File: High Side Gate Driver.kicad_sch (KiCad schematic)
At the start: 12 parts, among them U4 BQ76200PW

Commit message: worked on MCU
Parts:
- renumbered C46 to C21, C53 to C22, C55 to C23, R135 to R54, R138 to R55, R139 to R56, R140 to R57, R141 to R58, R142 to R59, R147 to R60, R148 to R61, U4 to U2
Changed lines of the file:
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@@
 		(on_board yes)
 		(dnp no)
-		(property "Reference" "R148"
+		(property "Reference" "R61"
 			(at 174.752 104.14 90)
 			(effects
@@
 			(project "Project-Star"
 				(path "/fc8533bc-25dd-4c20-9b4c-ffebebd6739b/e8da5d81-614b-4fe5-84b3-4c351fab7114/0c1979a3-247e-411f-a48d-22d4cf657d3e"
-					(reference "R148")
+					(reference "R61")
 					(unit 1)
 				)
@@
 		(on_board yes)
 		(dnp no)
-		(property "Reference" "#FLG06"
+		(property "Reference" "#FLG02"
 			(at 114.935 77.47 0)
 			(effects
@@
 			(project "Project-Star"
 				(path "/fc8533bc-25dd-4c20-9b4c-ffebebd6739b/e8da5d81-614b-4fe5-84b3-4c351fab7114/0c1979a3-247e-411f-a48d-22d4cf657d3e"
-					(reference "#FLG06")
+					(reference "#FLG02")
 					(unit 1)
 				)
@@
 		(on_board yes)
 		(dnp no)
-		(property "Reference" "#PWR079"
+		(property "Reference" "#PWR09"
 			(at 109.22 120.65 0)
 			(effects
@@
 			(project "Project-Star"
 				(path "/fc8533bc-25dd-4c20-9b4c-ffebebd6739b/e8da5d81-614b-4fe5-84b3-4c351fab7114/0c1979a3-247e-411f-a48d-22d4cf657d3e"
-					(reference "#PWR079")
+					(reference "#PWR09")
 					(unit 1)
 				)
@@
 		(on_board yes)
 		(dnp no)
-		(property "Reference" "C53"
+		(property "Reference" "C22"
 			(at 165.1 81.534 90)
 			(effects
@@
 			(project "Project-Star"
 				(path "/fc8533bc-25dd-4c20-9b4c-ffebebd6739b/e8da5d81-614b-4fe5-84b3-4c351fab7114/0c1979a3-247e-411f-a48d-22d4cf657d3e"
-					(reference "C53")
+					(reference "C22")
 					(unit 1)
 				)
@@
 		(on_board yes)
 		(dnp no)
-		(property "Reference" "R141"
+		(property "Reference" "R58"
 			(at 133.604 109.22 90)
 			(effects
@@
 			(project "Project-Star"
 				(path "/fc8533bc-25dd-4c20-9b4c-ffebebd6739b/e8da5d81-614b-4fe5-84b3-4c351fab7114/0c1979a3-247e-411f-a48d-22d4cf657d3e"
-					(reference "R141")
+					(reference "R58")
 					(unit 1)
 				)
@@
 		(on_board yes)
 		(dnp no)
-		(property "Reference" "#PWR081"
+		(property "Reference" "#PWR010"
 			(at 158.75 128.27 0)
 			(effects
@@
 			(project "Project-Star"
 				(path "/fc8533bc-25dd-4c20-9b4c-ffebebd6739b/e8da5d81-614b-4fe5-84b3-4c351fab7114/0c1979a3-247e-411f-a48d-22d4cf657d3e"
-					(reference "#PWR081")
+					(reference "#PWR010")
 					(unit 1)
 				)
@@
 		(on_board yes)
 		(dnp no)
-		(property "Reference" "R147"
+		(property "Reference" "R60"
 			(at 174.752 101.6 90)
 			(effects
@@
 			(project "Project-Star"
 				(path "/fc8533bc-25dd-4c20-9b4c-ffebebd6739b/e8da5d81-614b-4fe5-84b3-4c351fab7114/0c1979a3-247e-411f-a48d-22d4cf657d3e"
-					(reference "R147")
+					(reference "R60")
 					(unit 1)
 				)
@@
 		(on_board yes)
 		(dnp no)
-		(property "Reference" "R142"
+		(property "Reference" "R59"
 			(at 147.574 81.28 90)
 			(effects
@@
 			(project "Project-Star"
 				(path "/fc8533bc-25dd-4c20-9b4c-ffebebd6739b/e8da5d81-614b-4fe5-84b3-4c351fab7114/0c1979a3-247e-411f-a48d-22d4cf657d3e"
-					(reference "R142")
+					(reference "R59")
 					(unit 1)
 				)
@@
 		(on_board yes)
 		(dnp no)
-		(property "Reference" "#PWR057"
+		(property "Reference" "#PWR011"
 			(at 177.8 82.55 0)
 			(effects
@@
 			(project "Project-Star"
 				(path "/fc8533bc-25dd-4c20-9b4c-ffebebd6739b/e8da5d81-614b-4fe5-84b3-4c351fab7114/0c1979a3-247e-411f-a48d-22d4cf657d3e"
-					(reference "#PWR057")
+					(reference "#PWR011")
 					(unit 1)
 				)
@@
 		(on_board yes)
 		(dnp no)
-		(property "Reference" "#PWR012"
+		(property "Reference" "#PWR08"
 			(at 109.22 81.28 0)
 			(effects
@@
 			(project "Project-Star"
 				(path "/fc8533bc-25dd-4c20-9b4c-ffebebd6739b/e8da5d81-614b-4fe5-84b3-4c351fab7114/0c1979a3-247e-411f-a48d-22d4cf657d3e"
-					(reference "#PWR012")
+					(reference "#PWR08")
 					(unit 1)
 				)
@@
 		(on_board yes)
 		(dnp no)
-		(property "Reference" "C46"
+		(property "Reference" "C21"
 			(at 109.22 93.218 0)
 			(effects
@@
 			(project "Project-Star"
 				(path "/fc8533bc-25dd-4c20-9b4c-ffebebd6739b/e8da5d81-614b-4fe5-84b3-4c351fab7114/0c1979a3-247e-411f-a48d-22d4cf657d3e"
-					(reference "C46")
+					(reference "C21")
 					(unit 1)
 				)
@@
 		(on_board yes)
 		(dnp no)
-		(property "Reference" "R139"
+		(property "Reference" "R56"
 			(at 133.604 104.14 90)
 			(effects
@@
 			(project "Project-Star"
 				(path "/fc8533bc-25dd-4c20-9b4c-ffebebd6739b/e8da5d81-614b-4fe5-84b3-4c351fab7114/0c1979a3-247e-411f-a48d-22d4cf657d3e"
-					(reference "R139")
+					(reference "R56")
 					(unit 1)
 				)
@@
 		(on_board yes)
 		(dnp no)
-		(property "Reference" "#FLG05"
+		(property "Reference" "#FLG03"
 			(at 142.24 90.805 0)
 			(effects
@@
 			(project "Project-Star"
 				(path "/fc8533bc-25dd-4c20-9b4c-ffebebd6739b/e8da5d81-614b-4fe5-84b3-4c351fab7114/0c1979a3-247e-411f-a48d-22d4cf657d3e"
-					(reference "#FLG05")
+					(reference "#FLG03")
 					(unit 1)
 				)
@@
 		(on_board yes)
 		(dnp no)
-		(property "Reference" "R140"
+		(property "Reference" "R57"
 			(at 133.604 106.68 90)
 			(effects
@@
 			(project "Project-Star"
 				(path "/fc8533bc-25dd-4c20-9b4c-ffebebd6739b/e8da5d81-614b-4fe5-84b3-4c351fab7114/0c1979a3-247e-411f-a48d-22d4cf657d3e"
-					(reference "R140")
+					(reference "R57")
 					(unit 1)
 				)
@@
 		(on_board yes)
 		(dnp no)
-		(property "Reference" "R138"
+		(property "Reference" "R55"
 			(at 133.604 101.6 90)
 			(effects
@@
 			(project "Project-Star"
 				(path "/fc8533bc-25dd-4c20-9b4c-ffebebd6739b/e8da5d81-614b-4fe5-84b3-4c351fab7114/0c1979a3-247e-411f-a48d-22d4cf657d3e"
-					(reference "R138")
+					(reference "R55")
 					(unit 1)
 				)
@@
 		(on_board yes)
 		(dnp no)
-		(property "Reference" "C55"
+		(property "Reference" "C23"
 			(at 177.8 94.234 90)
 			(effects
@@
 			(project "Project-Star"
 				(path "/fc8533bc-25dd-4c20-9b4c-ffebebd6739b/e8da5d81-614b-4fe5-84b3-4c351fab7114/0c1979a3-247e-411f-a48d-22d4cf657d3e"
-					(reference "C55")
+					(reference "C23")
 					(unit 1)
 				)
@@
 		(on_board yes)
 		(dnp no)
-		(property "Reference" "R135"
+		(property "Reference" "R54"
 			(at 111.506 78.994 0)
 			(effects
@@
 			(project "Project-Star"
 				(path "/fc8533bc-25dd-4c20-9b4c-ffebebd6739b/e8da5d81-614b-4fe5-84b3-4c351fab7114/0c1979a3-247e-411f-a48d-22d4cf657d3e"
-					(reference "R135")
+					(reference "R54")
 					(unit 1)
 				)
@@
 		(on_board yes)
 		(dnp no)
-		(property "Reference" "U4"
+		(property "Reference" "U2"
 			(at 166.37 91.694 0)
 			(effects
@@
 			(project "Project-Star"
 				(path "/fc8533bc-25dd-4c20-9b4c-ffebebd6739b/e8da5d81-614b-4fe5-84b3-4c351fab7114/0c1979a3-247e-411f-a48d-22d4cf657d3e"
-					(reference "U4")
-					(unit 1)
-				)
+					(reference "U2")
+					(unit 1)
+				)

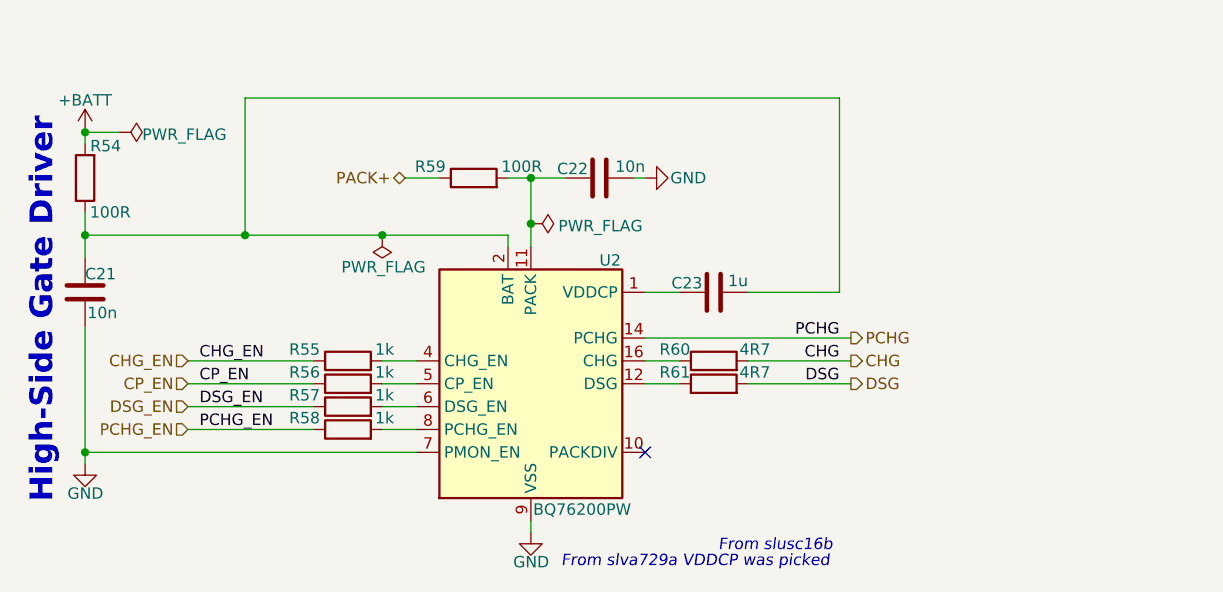
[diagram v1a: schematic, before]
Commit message: Added Fuel/Gas Guage
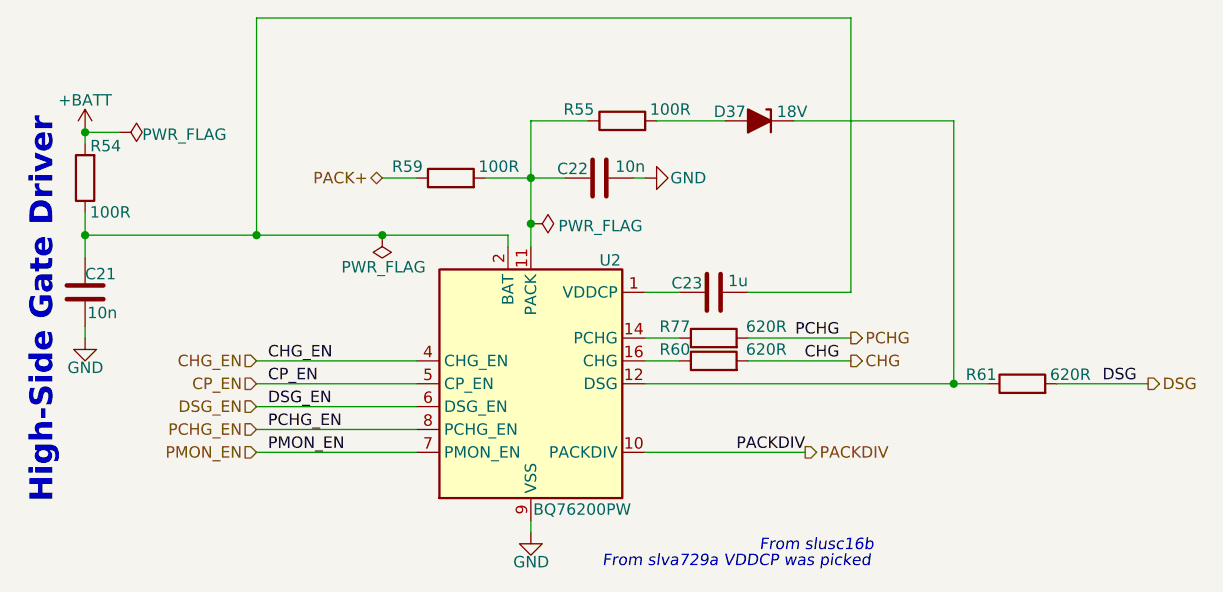
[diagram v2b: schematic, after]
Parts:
- removed R56, R57, R58: 1k, symbol Device:R
- added D37: 18V, symbol Device:D_Zener_Filled
- added R77: 620R, symbol Device:R
- R55: value 1k -> 100R
- R60, R61: value 4R7 -> 620R
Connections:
- net CHG_EN: now also U2.4 (CHG_EN); no longer R55.1
- net CP_EN: now also U2.5 (CP_EN)
- net DSG_EN: now also U2.6 (DSG_EN)
- net GND: no longer U2.7 (PMON_EN)
- net PCHG: now also R77.2; no longer U2.14 (PCHG)
- net PCHG_EN: now also U2.8 (PCHG_EN)
- net at R61.1, U2.12 (DSG): now also D37.1 (K)
- net at C22.1, R59.2, U2.11 (PACK): now also R55.1
- net at R55.2: now also D37.2 (A); no longer U2.4 (CHG_EN)
- net PACKDIV: now reaches U2.10 (PACKDIV)
- new net: R77.1, U2.14 (PCHG)
- new net PMON_EN: U2.7 (PMON_EN)
- no-connect marks 1 -> 0
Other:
- moved on the sheet: R59, R61
